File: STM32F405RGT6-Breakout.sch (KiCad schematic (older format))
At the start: 51 parts, among them J2 PWR OUT, J3 SWD/JTAG, J4 SPI1, J5 I2C1, J6 I2C2, J7 USART6, J8 USB_C_Receptacle_USB2.0, Q1 Si2301CDS, U1 STM32F405RGT6, U2 AMS1117-3.3, U3 IP4220CZ6

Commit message: the power flags thing is stupid
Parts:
- renumbered D2 to D1, D3 to D2, D1 to D3, J8 to J1, J7 to J4, J4 to J5, J5 to J6, J6 to J7
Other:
- note added: "Bleed off gate voltage \nif it rises to Vgs"
- note removed: "Bleed off gate voltage \nif it goes near Vgs"
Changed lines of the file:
@@
-$EndComp
-$Comp
-L Device:Ferrite_Bead_Small FB1
-U 1 1 619351E4
-P 3000 1350
-F 0 "FB1" V 2763 1350 50  0000 C CNN
-F 1 "100 @ 100 MHz" V 2854 1350 50  0000 C CNN
-F 2 "" V 2930 1350 50  0001 C CNN
-F 3 "~" H 3000 1350 50  0001 C CNN
-	1    3000 1350
-	0    1    1    0
-$EndComp
-$Comp
-L Device:Fuse_Small F1
-U 1 1 61935A18
-P 2400 1350
-F 0 "F1" H 2400 1535 50  0000 C CNN
-F 1 "500mA" H 2400 1444 50  0000 C CNN
-F 2 "" H 2400 1350 50  0001 C CNN
-F 3 "~" H 2400 1350 50  0001 C CNN
-	1    2400 1350
-	1    0    0    -1
-$EndComp
-$Comp
-L Device:D_Zener_Small D2
-U 1 1 61943D90
-P 2000 1500
-F 0 "D2" V 1954 1570 50  0000 L CNN
-F 1 "ZMM5V6" V 2045 1570 50  0000 L CNN
-F 2 "" V 2000 1500 50  0001 C CNN
-F 3 "~" V 2000 1500 50  0001 C CNN
-	1    2000 1500
-	0    1    1    0
 $EndComp
 $Comp
@@
 $EndComp
 Wire Wire Line
-	1600 1650 1600 1750
-Wire Wire Line
 	2000 1650 2000 1600
 Wire Wire Line
@@
 	1    0    0    -1
 $EndComp
-Wire Wire Line
-	950  1350 1400 1350
 Text Notes 1750 2200 0    50   ~ 0
 Throttle current through\nthe zener if polarity is reversed\n
-Wire Wire Line
-	2000 1350 1800 1350
-Wire Wire Line
-	2000 1350 2300 1350
 Text Notes 1900 1850 0    50   ~ 0
-Bleed off gate voltage \nif it goes near Vgs
+Bleed off gate voltage \nif it rises to Vgs
 $Comp
 L power:GND #PWR011
@@
 Wire Wire Line
 	4200 1350 4100 1350
-Wire Wire Line
-	2500 1350 2900 1350
 Text Notes 3050 1850 0    50   ~ 0
 Caps for stability\n
@@
 High frequency \nnoise filter\n
 Connection ~ 2000 1350
-$Comp
-L Device:Q_PMOS_SGD Q1
-U 1 1 61942650
-P 1600 1450
-F 0 "Q1" V 1942 1450 50  0000 C CNN
-F 1 "Si2301CDS" V 1851 1450 50  0000 C CNN
-F 2 "" H 1800 1550 50  0001 C CNN
-F 3 "~" H 1600 1450 50  0001 C CNN
-	1    1600 1450
-	0    -1   -1   0
-$EndComp
-Wire Wire Line
-	2000 1650 1600 1650
 Connection ~ 1600 1650
 Text Notes 2050 1100 0    50   ~ 0
@@
 	1    0    0    -1
 $EndComp
-Wire Wire Line
-	5350 5400 5350 5500
 Connection ~ 5350 5500
 $Comp
@@
 	1    0    0    -1
 $EndComp
-Wire Wire Line
-	1300 4300 1300 4100
 $Comp
 L power:GND #PWR03
@@
 	1150 5900 1000 5900
 $Comp
-L Device:LED_Small D1
+L Device:LED_Small D3
 U 1 1 61A9A358
 P 1250 5900
-F 0 "D1" H 1250 6135 50  0000 C CNN
+F 0 "D3" H 1250 6135 50  0000 C CNN
 F 1 "Red" H 1250 6044 50  0000 C CNN
 F 2 "" V 1250 5900 50  0001 C CNN
@@
 $EndComp
 $Comp
-L Device:LED_Small D3
+L Device:LED_Small D2
 U 1 1 61ABD2B2
 P 4650 1350
-F 0 "D3" H 4650 1143 50  0000 C CNN
+F 0 "D2" H 4650 1143 50  0000 C CNN
 F 1 "Red" H 4650 1234 50  0000 C CNN
 F 2 "" V 4650 1350 50  0001 C CNN
@@
 I2C1_SDA
 $Comp
-L Connector_Generic:Conn_01x04 J4
+L Connector_Generic:Conn_01x04 J5
 U 1 1 61C2CF63
 P 5550 2000
-F 0 "J4" H 5650 1900 50  0000 L CNN
+F 0 "J5" H 5650 1900 50  0000 L CNN
 F 1 "SPI1" H 5650 2000 50  0000 L CNN
 F 2 "" H 5550 2000 50  0001 C CNN
@@
 Wire Wire Line
 	3350 1650 3350 1750
-Wire Wire Line
-	3350 1750 3800 1750
-Wire Wire Line
-	3350 1350 3500 1350
 Connection ~ 3350 1350
 $Comp
@@
 	1    0    0    -1
 $EndComp
-Wire Wire Line
-	3100 1350 3350 1350
-$Comp
-L Connector_Generic:Conn_01x04 J5
+$Comp
+L Connector_Generic:Conn_01x04 J6
 U 1 1 61DAC74A
 P 5550 1200
-F 0 "J5" H 5650 1100 50  0000 L CNN
+F 0 "J6" H 5650 1100 50  0000 L CNN
 F 1 "I2C1" H 5650 1200 50  0000 L CNN
 F 2 "" H 5550 1200 50  0001 C CNN
@@
 $EndComp
 $Comp
-L Connector_Generic:Conn_01x04 J6
+L Connector_Generic:Conn_01x04 J7
 U 1 1 61DC0149
 P 6650 1200
-F 0 "J6" H 6750 1100 50  0000 L CNN
+F 0 "J7" H 6750 1100 50  0000 L CNN
 F 1 "I2C2" H 6750 1200 50  0000 L CNN
 F 2 "" H 6650 1200 50  0001 C CNN
@@
 $EndComp
 $Comp
-L Connector_Generic:Conn_01x04 J7
+L Connector_Generic:Conn_01x04 J4
 U 1 1 61DD83D6
 P 6650 1950
-F 0 "J7" H 6750 1850 50  0000 L CNN
+F 0 "J4" H 6750 1850 50  0000 L CNN
 F 1 "USART6" H 6750 1950 50  0000 L CNN
 F 2 "" H 6650 1950 50  0001 C CNN
@@
 	1    0    0    -1
 $EndComp
-$Comp
-L power:+5V #PWR01
-U 1 1 61F4F806
-P 950 1250
-F 0 "#PWR01" H 950 1100 50  0001 C CNN
-F 1 "+5V" H 965 1423 50  0000 C CNN
-F 2 "" H 950 1250 50  0001 C CNN
-F 3 "" H 950 1250 50  0001 C CNN
-	1    950  1250
-	1    0    0    -1
-$EndComp
 Wire Wire Line
 	950  1250 950  1350
@@
 L power:GND #PWR035
 U 1 1 61F61B97
-P 7050 4750
-F 0 "#PWR035" H 7050 4500 50  0001 C CNN
-F 1 "GND" H 7050 4600 50  0000 C CNN
-F 2 "" H 7050 4750 50  0001 C CNN
-F 3 "" H 7050 4750 50  0001 C CNN
-	1    7050 4750
-	1    0    0    -1
-$EndComp
-Wire Wire Line
-	7050 4650 7050 4750
+P 7050 4950
+F 0 "#PWR035" H 7050 4700 50  0001 C CNN
+F 1 "GND" H 7050 4800 50  0000 C CNN
+F 2 "" H 7050 4950 50  0001 C CNN
+F 3 "" H 7050 4950 50  0001 C CNN
+	1    7050 4950
+	1    0    0    -1
+$EndComp
 NoConn ~ 6750 4650
 Text GLabel 3300 4900 2    50   Input ~ 0
@@
 NoConn ~ 7650 4250
 NoConn ~ 7650 4350
-Text Notes 6200 4850 0    50   ~ 0
+Text Notes 6150 4700 0    50   ~ 0
 The shield is\ngrounded at \nthe host.
 $Comp
@@
 	1    0    0    -1
 $EndComp
-Wire Wire Line
-	7650 3150 8300 3150
 Wire Wire Line
 	8300 3150 8300 3100
@@
 $EndComp
 $Comp
-L Connector:USB_C_Receptacle_USB2.0 J8
+L Connector:USB_C_Receptacle_USB2.0 J1
 U 1 1 61DA89D1
 P 7050 3750
-F 0 "J8" H 7400 4500 50  0000 C CNN
+F 0 "J1" H 7400 4500 50  0000 C CNN
 F 1 "USB_C_Receptacle_USB2.0" H 7650 3000 50  0000 C CNN
 F 2 "" H 7200 3750 50  0001 C CNN
@@
 Text Notes 9100 3150 0    50   ~ 0
 Push spikes >5V up the ladder \nand shunt down to ground.\n(at least I think that's how it works)
+Wire Wire Line
+	1300 4100 1300 4300
+$Comp
+L power:+5V #PWR0101
+U 1 1 62154291
+P 950 1250
+F 0 "#PWR0101" H 950 1100 50  0001 C CNN
+F 1 "+5V" H 965 1423 50  0000 C CNN
+F 2 "" H 950 1250 50  0001 C CNN
+F 3 "" H 950 1250 50  0001 C CNN
+	1    950  1250
+	1    0    0    -1
+$EndComp
+Wire Wire Line
+	3350 1350 3500 1350
+Wire Wire Line
+	1600 1650 1600 1750
+Wire Wire Line
+	2000 1650 1600 1650
+Wire Wire Line
+	2000 1350 1800 1350
+$Comp
+L Device:D_Zener_Small D1
+U 1 1 61943D90
+P 2000 1500
+F 0 "D1" V 1954 1570 50  0000 L CNN
+F 1 "ZMM5V6" V 2045 1570 50  0000 L CNN
+F 2 "" V 2000 1500 50  0001 C CNN
+F 3 "~" V 2000 1500 50  0001 C CNN
+	1    2000 1500
+	0    1    1    0
+$EndComp
+Wire Wire Line
+	3100 1350 3350 1350
+$Comp
+L Device:Ferrite_Bead_Small FB1
+U 1 1 619351E4
+P 3000 1350
+F 0 "FB1" V 2763 1350 50  0000 C CNN
+F 1 "100 @ 100 MHz" V 2854 1350 50  0000 C CNN
+F 2 "" V 2930 1350 50  0001 C CNN
+F 3 "~" H 3000 1350 50  0001 C CNN
+	1    3000 1350
+	0    1    1    0
+$EndComp
+Wire Wire Line
+	950  1350 1400 1350
+Wire Wire Line
+	2000 1350 2300 1350
+Wire Wire Line
+	2500 1350 2700 1350
+$Comp
+L Device:Fuse_Small F1
+U 1 1 61935A18
+P 2400 1350
+F 0 "F1" H 2400 1535 50  0000 C CNN
+F 1 "500mA" H 2400 1444 50  0000 C CNN
+F 2 "" H 2400 1350 50  0001 C CNN
+F 3 "~" H 2400 1350 50  0001 C CNN
+	1    2400 1350
+	1    0    0    -1
+$EndComp
+$Comp
+L Device:Q_PMOS_SGD Q1
+U 1 1 61942650
+P 1600 1450
+F 0 "Q1" V 1942 1450 50  0000 C CNN
+F 1 "Si2301CDS" V 1851 1450 50  0000 C CNN
+F 2 "" H 1800 1550 50  0001 C CNN
+F 3 "~" H 1600 1450 50  0001 C CNN
+	1    1600 1450
+	0    -1   -1   0
+$EndComp
+Connection ~ 2700 1350
+Wire Wire Line
+	2700 1350 2900 1350
+Wire Wire Line
+	3350 1750 3800 1750
+Wire Wire Line
+	7650 3150 8300 3150
+Wire Wire Line
+	7050 4650 7050 4950
+Wire Wire Line
+	5350 5400 5350 5500
 $EndSCHEMATC

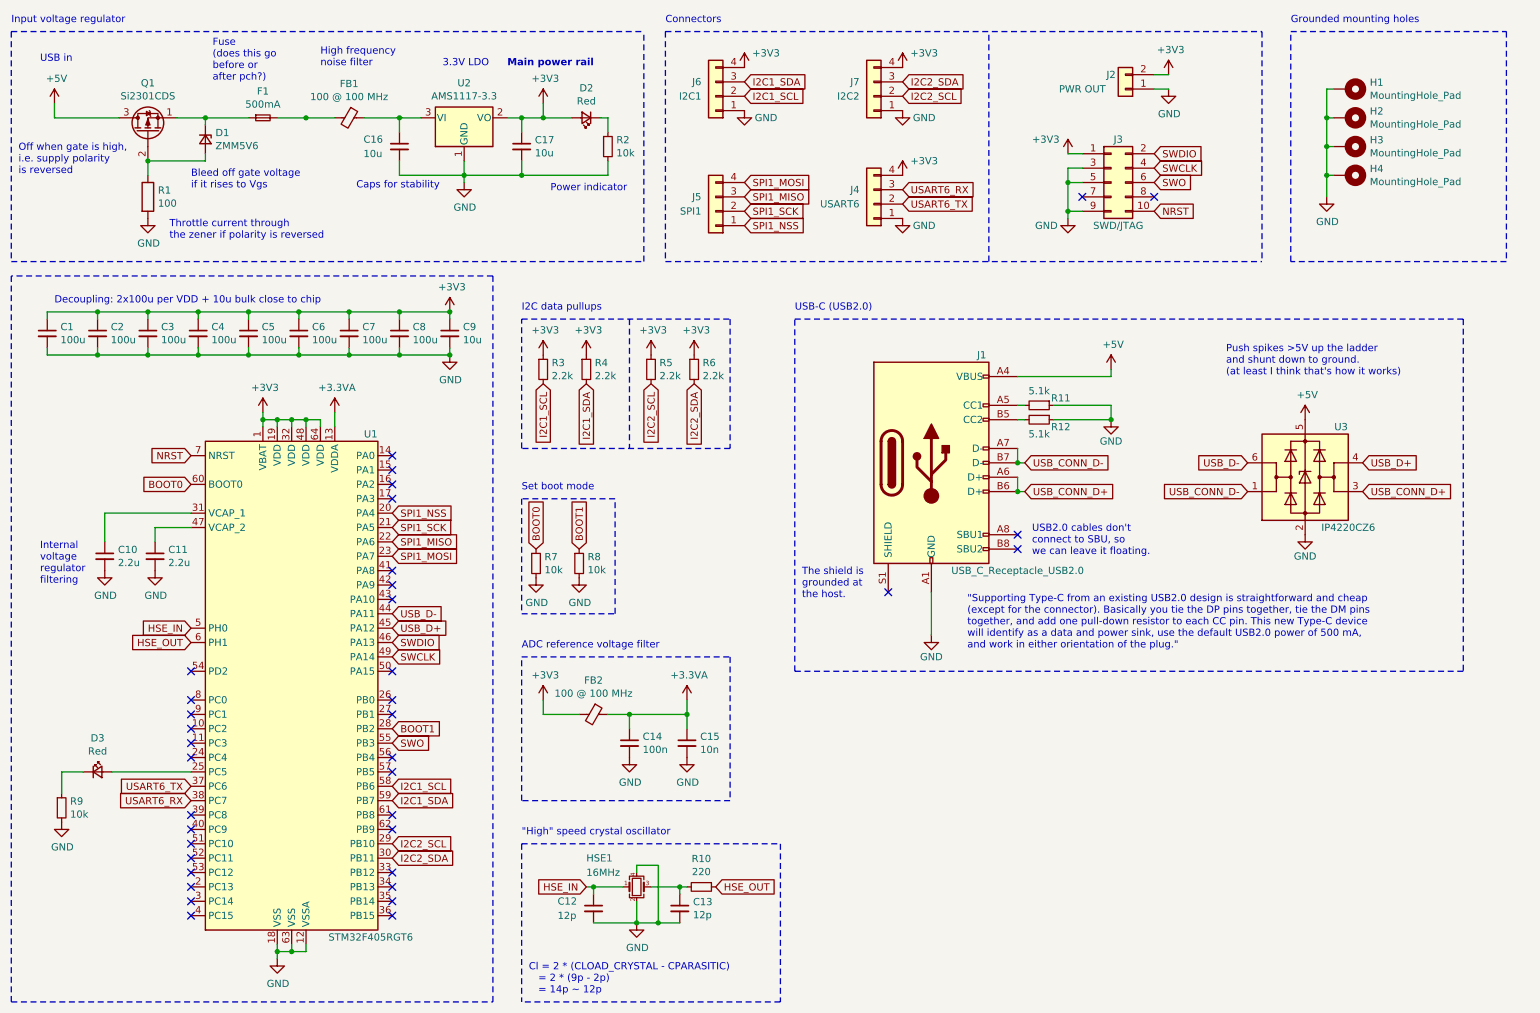
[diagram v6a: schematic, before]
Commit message: - Start assigning footprints for the major components   o  I was wrong about the pricing at JLCPCB; we don't have to buy a reel to do board assembly. - Still need to work out sizes for passives based on ESR/current
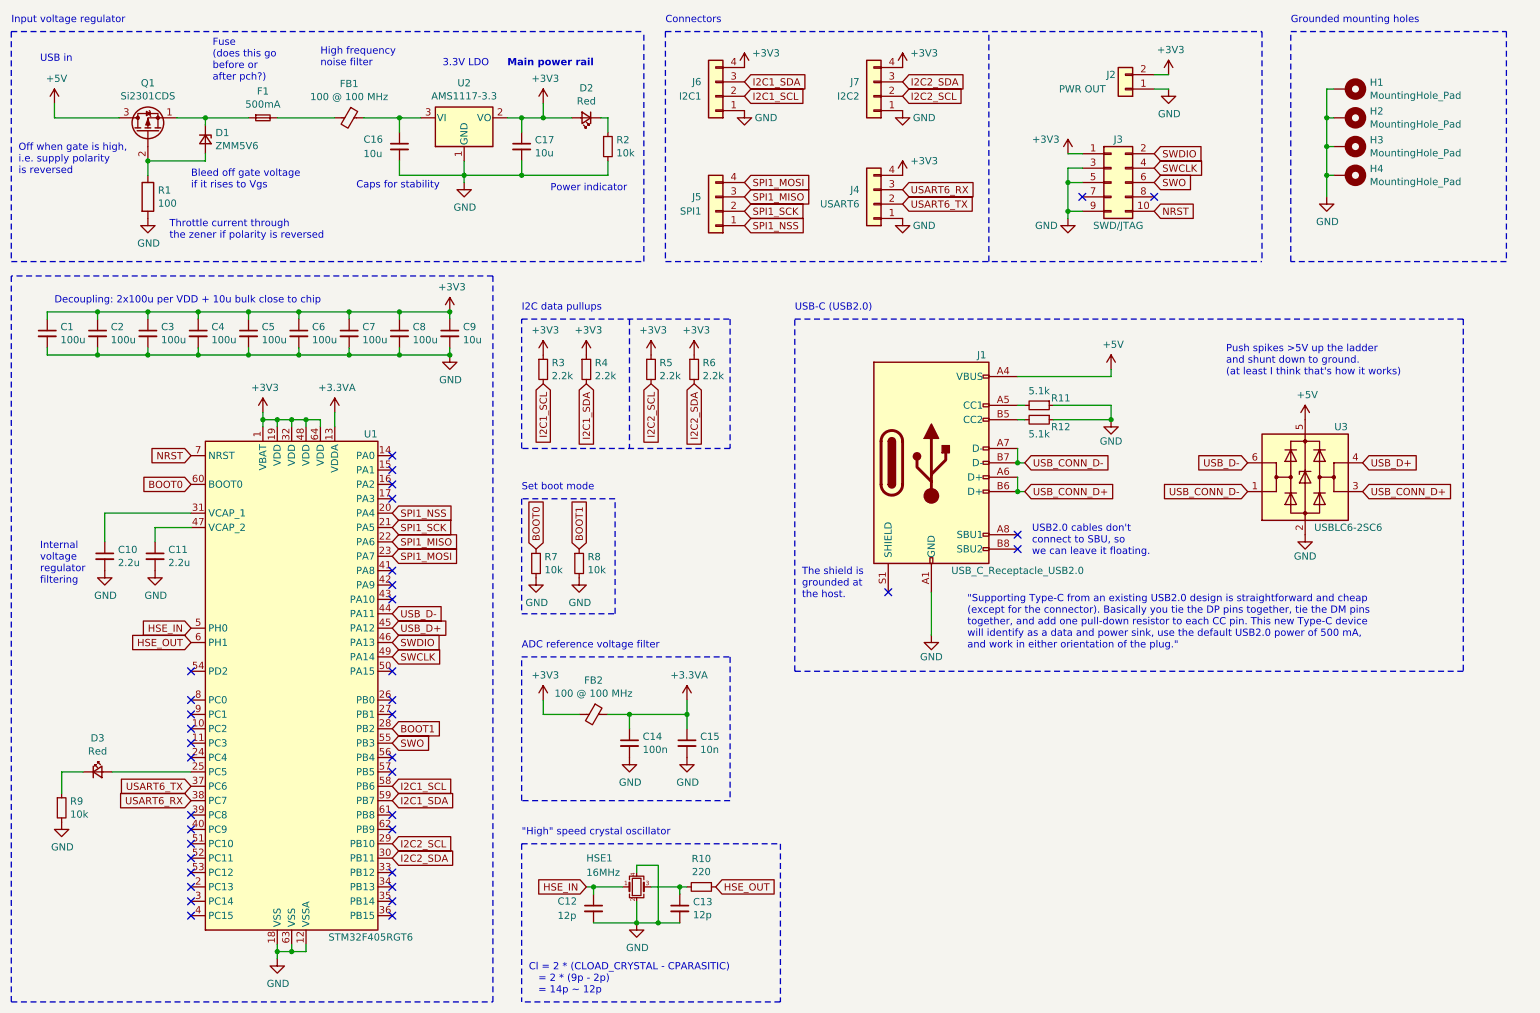
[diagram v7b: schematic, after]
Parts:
- H1, H2, H3, H4: footprint (none) -> MountingHole:MountingHole_3mm_Pad_Via
- HSE1: footprint (none) -> Crystal:Crystal_SMD_3225-4Pin_3.2x2.5mm
- J1: footprint (none) -> Connector_USB:USB_C_Receptacle_XKB_U262-16XN-4BVC11
- U3: value IP4220CZ6 -> USBLC6-2SC6
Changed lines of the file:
@@
 F 0 "HSE1" H 4650 6900 50  0000 L CNN
 F 1 "16MHz" H 4650 6800 50  0000 L CNN
-F 2 "" H 5000 6700 50  0001 C CNN
+F 2 "Crystal:Crystal_SMD_3225-4Pin_3.2x2.5mm" H 5000 6700 50  0001 C CNN
 F 3 "~" H 5000 6700 50  0001 C CNN
 	1    5000 6700
@@
 F 0 "H3" V 9904 1700 50  0000 L CNN
 F 1 "MountingHole_Pad" V 9995 1700 50  0000 L CNN
-F 2 "" H 9950 1550 50  0001 C CNN
+F 2 "MountingHole:MountingHole_3mm_Pad_Via" H 9950 1550 50  0001 C CNN
 F 3 "~" H 9950 1550 50  0001 C CNN
 	1    9950 1550
@@
 F 0 "H4" V 9904 1900 50  0000 L CNN
 F 1 "MountingHole_Pad" V 9995 1900 50  0000 L CNN
-F 2 "" H 9950 1750 50  0001 C CNN
+F 2 "MountingHole:MountingHole_3mm_Pad_Via" H 9950 1750 50  0001 C CNN
 F 3 "~" H 9950 1750 50  0001 C CNN
 	1    9950 1750
@@
 F 0 "H2" V 9904 1500 50  0000 L CNN
 F 1 "MountingHole_Pad" V 9995 1500 50  0000 L CNN
-F 2 "" H 9950 1350 50  0001 C CNN
+F 2 "MountingHole:MountingHole_3mm_Pad_Via" H 9950 1350 50  0001 C CNN
 F 3 "~" H 9950 1350 50  0001 C CNN
 	1    9950 1350
@@
 F 0 "H1" V 9904 1300 50  0000 L CNN
 F 1 "MountingHole_Pad" V 9995 1300 50  0000 L CNN
-F 2 "" H 9950 1150 50  0001 C CNN
+F 2 "MountingHole:MountingHole_3mm_Pad_Via" H 9950 1150 50  0001 C CNN
 F 3 "~" H 9950 1150 50  0001 C CNN
 	1    9950 1150
@@
 P 9650 3850
 F 0 "U3" H 9900 4200 50  0000 C CNN
-F 1 "IP4220CZ6 " H 9950 3500 50  0000 C CNN
+F 1 "USBLC6-2SC6" H 9950 3500 50  0000 C CNN
 F 2 "Package_TO_SOT_SMD:SOT-23-6" H 9650 3350 50  0001 C CNN
 F 3 "https://www.st.com/resource/en/datasheet/usblc6-2.pdf" H 9850 4200 50  0001 C CNN
@@
 F 0 "J1" H 7400 4500 50  0000 C CNN
 F 1 "USB_C_Receptacle_USB2.0" H 7650 3000 50  0000 C CNN
-F 2 "" H 7200 3750 50  0001 C CNN
+F 2 "Connector_USB:USB_C_Receptacle_XKB_U262-16XN-4BVC11" H 7200 3750 50  0001 C CNN
 F 3 "https://www.usb.org/sites/default/files/documents/usb_type-c.zip" H 7200 3750 50  0001 C CNN
 	1    7050 3750
@@
 Wire Wire Line
 	2000 1350 2300 1350
-Wire Wire Line
-	2500 1350 2700 1350
 $Comp
 L Device:Fuse_Small F1
@@
 	0    -1   -1   0
 $EndComp
-Connection ~ 2700 1350
-Wire Wire Line
-	2700 1350 2900 1350
 Wire Wire Line
 	3350 1750 3800 1750
@@
 Wire Wire Line
 	5350 5400 5350 5500
+Wire Wire Line
+	2500 1350 2900 1350
 $EndSCHEMATC

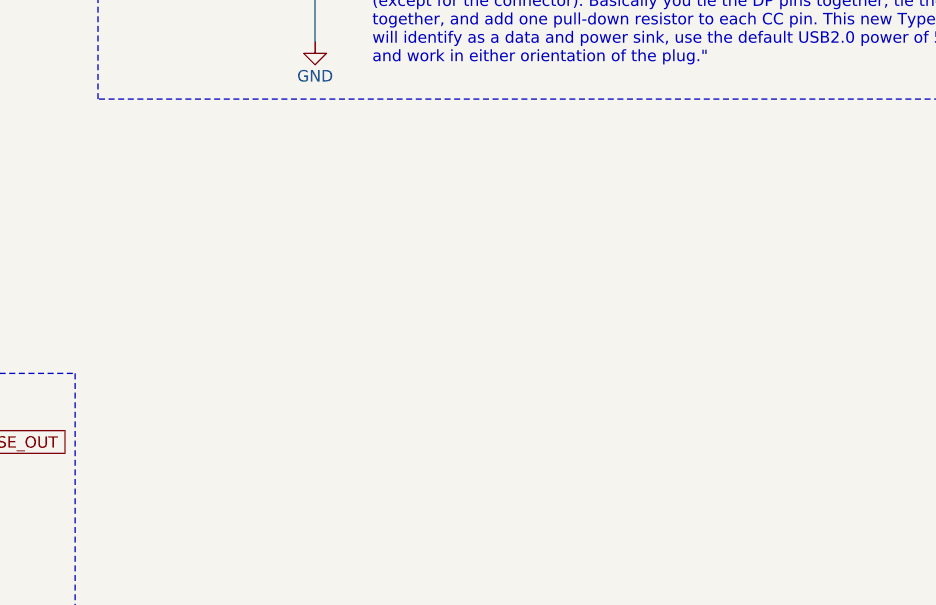
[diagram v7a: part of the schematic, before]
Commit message: Started adding a 128mb NOR flash, but eh... why? They're basic parts at JLCPCB so it might be worth it just to try interfacing with it and see what's going on there. It seems pretty idiot proof hardware wise though.
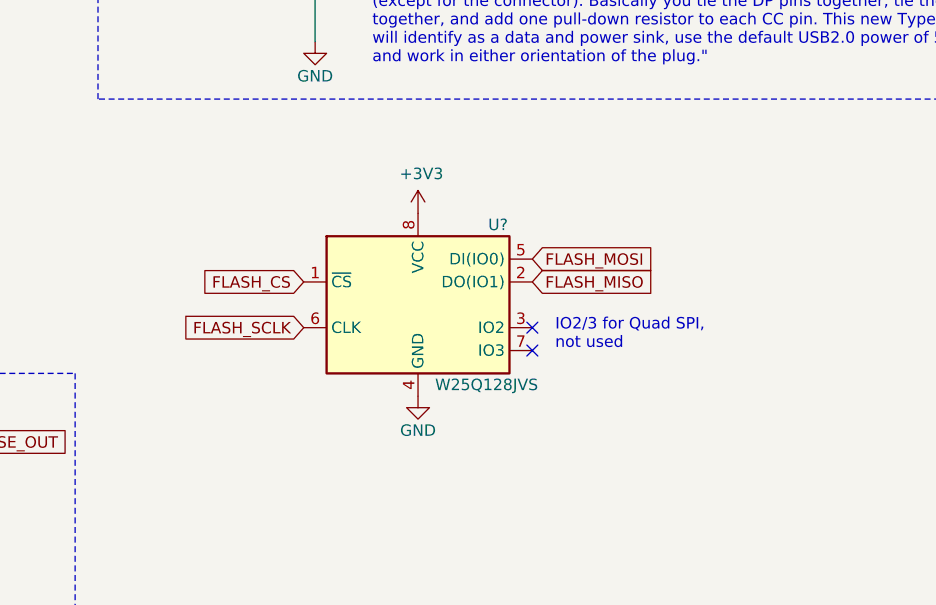
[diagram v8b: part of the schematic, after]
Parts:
- added U?: W25Q128JVS, Package_SO:SOIC-8_5.23x5.23mm_P1.27mm, symbol Memory_Flash:W25Q128JVS
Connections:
- net +3V3: now also U?.8 (VCC)
- net GND: now also U?.4 (GND)
- new net FLASH_CS: U?.1 (~CS)
- new net FLASH_MISO: U?.2 (DO(IO1))
- new net FLASH_MOSI: U?.5 (DI(IO0))
- new net FLASH_SCLK: U?.6 (CLK)
- no-connect marks 37 -> 39
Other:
- note added: "IO2/3 for Quad SPI,\nnot used"
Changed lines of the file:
@@
 Wire Wire Line
 	2500 1350 2900 1350
+$Comp
+L Memory_Flash:W25Q128JVS U?
+U 1 1 61978862
+P 7500 6100
+F 0 "U?" H 7850 6450 50  0000 C CNN
+F 1 "W25Q128JVS" H 7800 5750 50  0000 C CNN
+F 2 "Package_SO:SOIC-8_5.23x5.23mm_P1.27mm" H 7500 6100 50  0001 C CNN
+F 3 "http://www.winbond.com/resource-files/w25q128jv_dtr%20revc%2003272018%20plus.pdf" H 7500 6100 50  0001 C CNN
+	1    7500 6100
+	1    0    0    -1
+$EndComp
+$Comp
+L power:GND #PWR?
+U 1 1 6197D247
+P 7500 6500
+F 0 "#PWR?" H 7500 6250 50  0001 C CNN
+F 1 "GND" H 7500 6350 50  0000 C CNN
+F 2 "" H 7500 6500 50  0001 C CNN
+F 3 "" H 7500 6500 50  0001 C CNN
+	1    7500 6500
+	1    0    0    -1
+$EndComp
+$Comp
+L power:+3V3 #PWR?
+U 1 1 6197DBCF
+P 7500 5700
+F 0 "#PWR?" H 7500 5550 50  0001 C CNN
+F 1 "+3V3" H 7515 5873 50  0000 C CNN
+F 2 "" H 7500 5700 50  0001 C CNN
+F 3 "" H 7500 5700 50  0001 C CNN
+	1    7500 5700
+	1    0    0    -1
+$EndComp
+Text GLabel 7000 6000 0    50   Input ~ 0
+FLASH_CS
+Text GLabel 7000 6200 0    50   Input ~ 0
+FLASH_SCLK
+Text GLabel 8000 5900 2    50   Input ~ 0
+FLASH_MOSI
+Text GLabel 8000 6000 2    50   Input ~ 0
+FLASH_MISO
+NoConn ~ 8000 6200
+NoConn ~ 8000 6300
+Text Notes 8100 6300 0    50   ~ 0
+IO2/3 for Quad SPI,\nnot used
 $EndSCHEMATC
